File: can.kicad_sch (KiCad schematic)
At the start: 13 parts, among them U6 TJA1051T/3

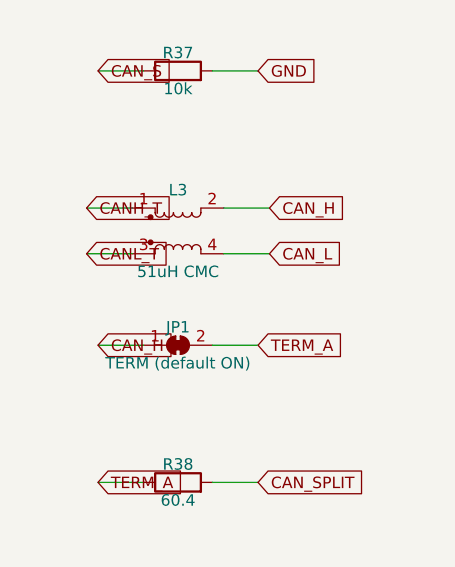
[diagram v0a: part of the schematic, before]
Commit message: Pass ERC clean on KiCad 9.0 and regenerate against its libraries
- Add a PWR_FLAG on VBAT_FB so the LM74700 ANODE power-input pin, fed
  through the reverse-battery FET and EMI bead, no longer trips
  power_pin_not_driven.
- Resolve the generic MOSFET symbols from Transistor_FET where the
  KiCad 9 libraries moved them out of Device.
- Handle the KiCad 9 library format in the raw-symbol extractor: tab
  indentation, CRLF line endings, and no trailing space after the
  symbol name.
- Flatten derived symbols the way KiCad does — carry the child's whole
  property blocks into the parent geometry instead of only swapping the
  value strings — so the embedded USBLC6-2SC6 matches the library copy.
- Regenerate all sheets, netlist, and the PDF plot; embedded symbol
  definitions now come from the KiCad 9.0 (20241209) libraries.

Validated with kicad-cli 9.0: all sheets load, connectivity matches
netlist.txt on 102 nets / 153 instances, ERC clean.

Co-Authored-By: Claude Fable 5 <noreply@anthropic.com>
Claude-Session: https://claude.ai/code/session_01DhNbL25h25p8VFCjRfJik9
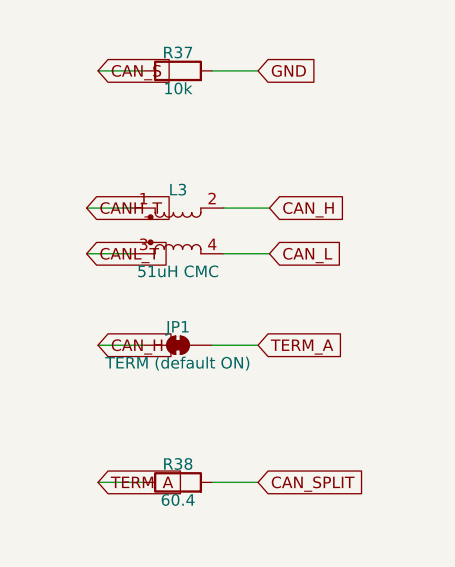
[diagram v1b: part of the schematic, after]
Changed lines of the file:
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@@
+    (stroke (width 0) (type default))
+  )
+  (wire (pts (xy 46.99 30.48) (xy 41.91 30.48))
+    (stroke (width 0) (type default))
+  )
+  (wire (pts (xy 46.99 35.56) (xy 41.91 35.56))
+    (stroke (width 0) (type default))
+  )
+  (wire (pts (xy 46.99 38.1) (xy 41.91 38.1))
+    (stroke (width 0) (type default))
+  )
+  (wire (pts (xy 59.69 22.86) (xy 59.69 17.78))
     (stroke (width 0) (type default))
   )
@@
     (stroke (width 0) (type default))
   )
-  (wire (pts (xy 59.69 22.86) (xy 59.69 17.78))
-    (stroke (width 0) (type default))
-  )
-  (wire (pts (xy 46.99 30.48) (xy 41.91 30.48))
-    (stroke (width 0) (type default))
-  )
-  (wire (pts (xy 46.99 35.56) (xy 41.91 35.56))
+  (wire (pts (xy 72.39 30.48) (xy 77.47 30.48))
     (stroke (width 0) (type default))
   )
@@
     (stroke (width 0) (type default))
   )
-  (wire (pts (xy 72.39 30.48) (xy 77.47 30.48))
-    (stroke (width 0) (type default))
-  )
-  (wire (pts (xy 46.99 38.1) (xy 41.91 38.1))
-    (stroke (width 0) (type default))
-  )
   (wire (pts (xy 55.88 55.88) (xy 50.8 55.88))
     (stroke (width 0) (type default))
@@
     (stroke (width 0) (type default))
   )
+  (wire (pts (xy 54.61 106.68) (xy 49.53 106.68))
+    (stroke (width 0) (type default))
+  )
   (wire (pts (xy 64.77 101.6) (xy 69.85 101.6))
     (stroke (width 0) (type default))
   )
-  (wire (pts (xy 54.61 106.68) (xy 49.53 106.68))
-    (stroke (width 0) (type default))
-  )
   (wire (pts (xy 64.77 106.68) (xy 69.85 106.68))
     (stroke (width 0) (type default))
@@
     )
   )
+  (global_label "CAN_RX" (shape input) (at 41.91 30.48 180) (fields_autoplaced)
+    (effects (font (size 1.27 1.27)) (justify left))
+    (property "Intersheet References" "${INTERSHEET_REFS}" (at 41.91 30.48 0)
+      (effects (font (size 1.27 1.27)) (justify left) hide)
+    )
+  )
+  (global_label "+3V3" (shape input) (at 41.91 35.56 180) (fields_autoplaced)
+    (effects (font (size 1.27 1.27)) (justify left))
+    (property "Intersheet References" "${INTERSHEET_REFS}" (at 41.91 35.56 0)
+      (effects (font (size 1.27 1.27)) (justify left) hide)
+    )
+  )
+  (global_label "CAN_S" (shape input) (at 41.91 38.1 180) (fields_autoplaced)
+    (effects (font (size 1.27 1.27)) (justify left))
+    (property "Intersheet References" "${INTERSHEET_REFS}" (at 41.91 38.1 0)
+      (effects (font (size 1.27 1.27)) (justify left) hide)
+    )
+  )
+  (global_label "+5V" (shape input) (at 59.69 17.78 90) (fields_autoplaced)
+    (effects (font (size 1.27 1.27)) (justify left))
+    (property "Intersheet References" "${INTERSHEET_REFS}" (at 59.69 17.78 0)
+      (effects (font (size 1.27 1.27)) (justify left) hide)
+    )
+  )
   (global_label "GND" (shape input) (at 59.69 48.26 270) (fields_autoplaced)
     (effects (font (size 1.27 1.27)) (justify left))
@@
     )
   )
-  (global_label "+5V" (shape input) (at 59.69 17.78 90) (fields_autoplaced)
-    (effects (font (size 1.27 1.27)) (justify left))
-    (property "Intersheet References" "${INTERSHEET_REFS}" (at 59.69 17.78 0)
-      (effects (font (size 1.27 1.27)) (justify left) hide)
-    )
-  )
-  (global_label "CAN_RX" (shape input) (at 41.91 30.48 180) (fields_autoplaced)
-    (effects (font (size 1.27 1.27)) (justify left))
-    (property "Intersheet References" "${INTERSHEET_REFS}" (at 41.91 30.48 0)
-      (effects (font (size 1.27 1.27)) (justify left) hide)
-    )
-  )
-  (global_label "+3V3" (shape input) (at 41.91 35.56 180) (fields_autoplaced)
-    (effects (font (size 1.27 1.27)) (justify left))
-    (property "Intersheet References" "${INTERSHEET_REFS}" (at 41.91 35.56 0)
+  (global_label "CANH_T" (shape input) (at 77.47 30.48 0) (fields_autoplaced)
+    (effects (font (size 1.27 1.27)) (justify left))
+    (property "Intersheet References" "${INTERSHEET_REFS}" (at 77.47 30.48 0)
       (effects (font (size 1.27 1.27)) (justify left) hide)
     )
@@
     )
   )
-  (global_label "CANH_T" (shape input) (at 77.47 30.48 0) (fields_autoplaced)
-    (effects (font (size 1.27 1.27)) (justify left))
-    (property "Intersheet References" "${INTERSHEET_REFS}" (at 77.47 30.48 0)
-      (effects (font (size 1.27 1.27)) (justify left) hide)
-    )
-  )
-  (global_label "CAN_S" (shape input) (at 41.91 38.1 180) (fields_autoplaced)
-    (effects (font (size 1.27 1.27)) (justify left))
-    (property "Intersheet References" "${INTERSHEET_REFS}" (at 41.91 38.1 0)
-      (effects (font (size 1.27 1.27)) (justify left) hide)
-    )
-  )
   (global_label "+5V" (shape input) (at 50.8 55.88 180) (fields_autoplaced)
     (effects (font (size 1.27 1.27)) (justify left))
@@
     )
   )
+  (global_label "CANL_T" (shape input) (at 49.53 106.68 180) (fields_autoplaced)
+    (effects (font (size 1.27 1.27)) (justify left))
+    (property "Intersheet References" "${INTERSHEET_REFS}" (at 49.53 106.68 0)
+      (effects (font (size 1.27 1.27)) (justify left) hide)
+    )
+  )
   (global_label "CAN_H" (shape input) (at 69.85 101.6 0) (fields_autoplaced)
     (effects (font (size 1.27 1.27)) (justify left))
     (property "Intersheet References" "${INTERSHEET_REFS}" (at 69.85 101.6 0)
-      (effects (font (size 1.27 1.27)) (justify left) hide)
-    )
-  )
-  (global_label "CANL_T" (shape input) (at 49.53 106.68 180) (fields_autoplaced)
-    (effects (font (size 1.27 1.27)) (justify left))
-    (property "Intersheet References" "${INTERSHEET_REFS}" (at 49.53 106.68 0)
       (effects (font (size 1.27 1.27)) (justify left) hide)
     )
@@
     )
     (pin "1")
-    (pin "2")
-    (pin "3")
     (pin "4")
     (pin "5")
+    (pin "8")
+    (pin "3")
+    (pin "2")
+    (pin "7")
     (pin "6")
-    (pin "7")
-    (pin "8")
     (instances
       (project "esp32s3-can-sd-logger"
@@
     )
     (pin "1")
+    (pin "3")
     (pin "2")
-    (pin "3")
     (pin "4")
     (instances

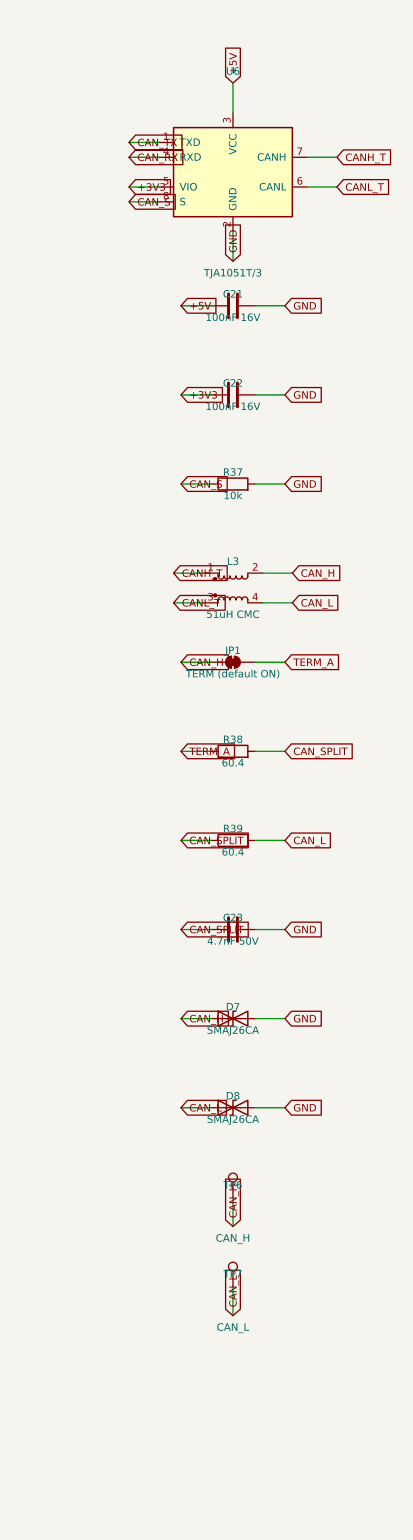
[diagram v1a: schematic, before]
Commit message: Fix the LM5164 power stages against the datasheet and TI's DDA drawing
Review of datasheet SNVSAU4D and package drawing 4214849/B (DDA0008B)
caught five issues, all fixed and re-verified:

- RON placeholders (100k -> ~125/83kHz) corrected to 31.6k (396kHz, 5V)
  and 20.5k (402kHz, 3V3); minimum on-time at the 53.3V clamp is
  237ns/154ns, well above the 50ns floor.
- Bootstrap caps were 100nF; the datasheet mandates exactly 2.2nF and
  warns larger values damage the internal VCC regulator. Now 2.2nF 50V.
- No FB ripple injection on the all-ceramic outputs -- a COT stability
  requirement (Table 6-1). Added Type-3 networks (RA/CA/CB: 121k and
  95.3k / 3.3nF / 270pF) sized for ~20mV ramp at 14V per TI's example.
- Exposed-pad footprint EP2.41x3.3mm was smaller than the DDA0008B pad
  itself (max 2.71x3.4mm); swapped to the EP2.95x4.9mm_Mask2.71x3.4mm
  footprint matching TI's example land pattern.
- Quantified BAT54S back-feed into +3V3: one input shorted to battery
  floats the rail to ~3.6V when the MCU sleeps. Added D2, an MM3Z3V6T1G
  3.6V zener rail clamp.

Load-dump assumption confirmed by the owner: alternator never exceeds
20V, so the SMCJ33A standoff has comfortable margin.

Validated with kicad-cli 9.0: 104 nets / 160 instances match, ERC clean.

Co-Authored-By: Claude Fable 5 <noreply@anthropic.com>
Claude-Session: https://claude.ai/code/session_01DhNbL25h25p8VFCjRfJik9
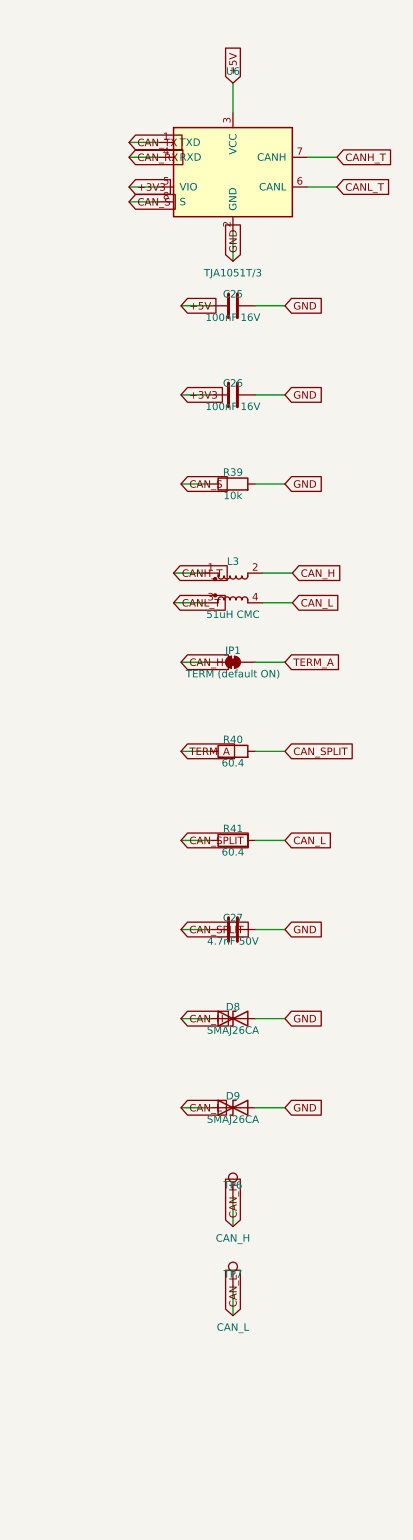
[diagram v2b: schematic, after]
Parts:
- removed C21, C22: 100nF 16V, Capacitor_SMD:C_0805_2012Metric, symbol Device:C
- removed C23: 4.7nF 50V, Capacitor_SMD:C_0805_2012Metric, symbol Device:C
- removed D7: SMAJ26CA, Diode_SMD:D_SMA, symbol Device:D_TVS
- removed R37: 10k, Resistor_SMD:R_0805_2012Metric, symbol Device:R
- removed R38: 60.4, Resistor_SMD:R_0805_2012Metric, symbol Device:R
- added C25, C26: 100nF 16V, Capacitor_SMD:C_0805_2012Metric, symbol Device:C
- added C27: 4.7nF 50V, Capacitor_SMD:C_0805_2012Metric, symbol Device:C
- added D9: SMAJ26CA, Diode_SMD:D_SMA, symbol Device:D_TVS
- added R40, R41: 60.4, Resistor_SMD:R_0805_2012Metric, symbol Device:R
- D8: Note (none) -> Bidirectional bus clamp
- R39: value 60.4 -> 10k; Note Split termination lower half -> Default to normal (non-silent) mode
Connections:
- net +3V3: now also C26.1
- net +5V: now also C25.1
- net CAN_H: now also D8.1 (A1)
- net CAN_L: now also D9.1 (A1), R41.2; no longer D8.1 (A1), R39.2
- net CAN_S: now also R39.1
- net CAN_SPLIT: now also C27.1, R40.2, R41.1; no longer R39.1
- net GND: now also R39.2, C25.2, C26.2, C27.2, D9.2 (A2)
- net TERM_A: now also R40.1
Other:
- moved on the sheet: D8, R39
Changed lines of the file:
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@@
   (symbol (lib_id "Device:C") (at 59.69 55.88 90) (unit 1)
     (in_bom yes) (on_board yes) (dnp no)
-    (property "Reference" "C21" (at 59.69 53.88 270)
+    (property "Reference" "C25" (at 59.69 53.88 270)
       (effects (font (size 1.27 1.27)) )
     )
@@
     (instances
       (project "esp32s3-can-sd-logger"
-        (path "/3276c6e6-7085-5954-8442-c6cef7eab316/de4828a4-9871-500a-b45f-afe12f432271" (reference "C21") (unit 1))
+        (path "/3276c6e6-7085-5954-8442-c6cef7eab316/de4828a4-9871-500a-b45f-afe12f432271" (reference "C25") (unit 1))
       )
     )
@@
   (symbol (lib_id "Device:C") (at 59.69 71.12 90) (unit 1)
     (in_bom yes) (on_board yes) (dnp no)
-    (property "Reference" "C22" (at 59.69 69.12 270)
+    (property "Reference" "C26" (at 59.69 69.12 270)
       (effects (font (size 1.27 1.27)) )
     )
@@
     (instances
       (project "esp32s3-can-sd-logger"
-        (path "/3276c6e6-7085-5954-8442-c6cef7eab316/de4828a4-9871-500a-b45f-afe12f432271" (reference "C22") (unit 1))
+        (path "/3276c6e6-7085-5954-8442-c6cef7eab316/de4828a4-9871-500a-b45f-afe12f432271" (reference "C26") (unit 1))
       )
     )
@@
   (symbol (lib_id "Device:R") (at 59.69 86.36 90) (unit 1)
     (in_bom yes) (on_board yes) (dnp no)
-    (property "Reference" "R37" (at 59.69 84.36 270)
+    (property "Reference" "R39" (at 59.69 84.36 270)
       (effects (font (size 1.27 1.27)) )
     )
@@
     (instances
       (project "esp32s3-can-sd-logger"
-        (path "/3276c6e6-7085-5954-8442-c6cef7eab316/de4828a4-9871-500a-b45f-afe12f432271" (reference "R37") (unit 1))
+        (path "/3276c6e6-7085-5954-8442-c6cef7eab316/de4828a4-9871-500a-b45f-afe12f432271" (reference "R39") (unit 1))
       )
     )
@@
   (symbol (lib_id "Device:R") (at 59.69 132.08 90) (unit 1)
     (in_bom yes) (on_board yes) (dnp no)
-    (property "Reference" "R38" (at 59.69 130.08 270)
+    (property "Reference" "R40" (at 59.69 130.08 270)
       (effects (font (size 1.27 1.27)) )
     )
@@
     (instances
       (project "esp32s3-can-sd-logger"
-        (path "/3276c6e6-7085-5954-8442-c6cef7eab316/de4828a4-9871-500a-b45f-afe12f432271" (reference "R38") (unit 1))
+        (path "/3276c6e6-7085-5954-8442-c6cef7eab316/de4828a4-9871-500a-b45f-afe12f432271" (reference "R40") (unit 1))
       )
     )
@@
   (symbol (lib_id "Device:R") (at 59.69 147.32 90) (unit 1)
     (in_bom yes) (on_board yes) (dnp no)
-    (property "Reference" "R39" (at 59.69 145.32 270)
+    (property "Reference" "R41" (at 59.69 145.32 270)
       (effects (font (size 1.27 1.27)) )
     )
@@
     (instances
       (project "esp32s3-can-sd-logger"
-        (path "/3276c6e6-7085-5954-8442-c6cef7eab316/de4828a4-9871-500a-b45f-afe12f432271" (reference "R39") (unit 1))
+        (path "/3276c6e6-7085-5954-8442-c6cef7eab316/de4828a4-9871-500a-b45f-afe12f432271" (reference "R41") (unit 1))
       )
     )
@@
   (symbol (lib_id "Device:C") (at 59.69 162.56 90) (unit 1)
     (in_bom yes) (on_board yes) (dnp no)
-    (property "Reference" "C23" (at 59.69 160.56 270)
+    (property "Reference" "C27" (at 59.69 160.56 270)
       (effects (font (size 1.27 1.27)) )
     )
@@
     (instances
       (project "esp32s3-can-sd-logger"
-        (path "/3276c6e6-7085-5954-8442-c6cef7eab316/de4828a4-9871-500a-b45f-afe12f432271" (reference "C23") (unit 1))
+        (path "/3276c6e6-7085-5954-8442-c6cef7eab316/de4828a4-9871-500a-b45f-afe12f432271" (reference "C27") (unit 1))
       )
     )
@@
   (symbol (lib_id "Device:D_TVS") (at 59.69 177.8 0) (unit 1)
     (in_bom yes) (on_board yes) (dnp no)
-    (property "Reference" "D7" (at 59.69 175.8 0)
+    (property "Reference" "D8" (at 59.69 175.8 0)
       (effects (font (size 1.27 1.27)) )
     )
@@
     (instances
       (project "esp32s3-can-sd-logger"
-        (path "/3276c6e6-7085-5954-8442-c6cef7eab316/de4828a4-9871-500a-b45f-afe12f432271" (reference "D7") (unit 1))
+        (path "/3276c6e6-7085-5954-8442-c6cef7eab316/de4828a4-9871-500a-b45f-afe12f432271" (reference "D8") (unit 1))
       )
     )
@@
   (symbol (lib_id "Device:D_TVS") (at 59.69 193.04 0) (unit 1)
     (in_bom yes) (on_board yes) (dnp no)
-    (property "Reference" "D8" (at 59.69 191.04 0)
+    (property "Reference" "D9" (at 59.69 191.04 0)
       (effects (font (size 1.27 1.27)) )
     )
@@
     (instances
       (project "esp32s3-can-sd-logger"
-        (path "/3276c6e6-7085-5954-8442-c6cef7eab316/de4828a4-9871-500a-b45f-afe12f432271" (reference "D8") (unit 1))
-      )
-    )
+        (path "/3276c6e6-7085-5954-8442-c6cef7eab316/de4828a4-9871-500a-b45f-afe12f432271" (reference "D9") (unit 1))
+      )
+    )

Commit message: Generate the 4-layer board: placed, DRC-clean, ready to route
gen/generate_pcb.py (runs under KiCad 9's bundled Python) builds
esp32s3-can-sd-logger.kicad_pcb from the same part/net tables as the
schematic generator: real library footprints, every pad netted, and
zone-based placement -- harness connectors on the left edge, analog
channel columns and the ESP32 with its antenna overhanging the top edge
(module keepout falls off-board), USB-C/microSD/buttons on the right,
battery front end and both bucks in the bottom band, GND and +3V3
inner-plane zones, JLC-compatible 0.2mm minimum drill.

84 x 72 mm. kicad-cli pcb drc: zero violations; the 335 unconnected
items are the unrouted ratsnest.

Also adds the project footprint library (TDK ACT45B CAN choke built from
the datasheet land pattern) and a placement render under plots/.

Co-Authored-By: Claude Fable 5 <noreply@anthropic.com>
Claude-Session: https://claude.ai/code/session_01DhNbL25h25p8VFCjRfJik9
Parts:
- L3: footprint Inductor_SMD:L_CommonMode_Wuerth_WE-SL2 -> esp32autosport:L_CommonMode_TDK_ACT45B; MPN Wurth 744232222 -> TDK ACT45B-510-2P-TL003; Note Common-mode choke on the bus side -> AEC-Q200 CAN choke; footprint pads renumbered so symbol win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
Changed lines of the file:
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@@
       (effects (font (size 1.27 1.27)) )
     )
-    (property "Footprint" "Inductor_SMD:L_CommonMode_Wuerth_WE-SL2" (at 59.69 108.68 0)
+    (property "Footprint" "esp32autosport:L_CommonMode_TDK_ACT45B" (at 59.69 108.68 0)
       (effects (font (size 1.27 1.27)) hide)
     )
@@
       (effects (font (size 1.27 1.27)) hide)
     )
-    (property "MPN" "Wurth 744232222" (at 59.69 108.68 0)
+    (property "MPN" "TDK ACT45B-510-2P-TL003" (at 59.69 108.68 0)
       (effects (font (size 1.27 1.27)) hide)
     )
-    (property "Note" "Common-mode choke on the bus side" (at 59.69 108.68 0)
+    (property "Note" "AEC-Q200 CAN choke; footprint pads renumbered so symbol winding 1-2 is the package's top (1-4) winding" (at 59.69 108.68 0)
       (effects (font (size 1.27 1.27)) hide)
     )
